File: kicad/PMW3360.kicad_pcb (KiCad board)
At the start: 2 copper layers, 22 x 34 mm, 12 parts, among them J1 Conn_01x07, U1 PMW3360, U2 TCR2EF19

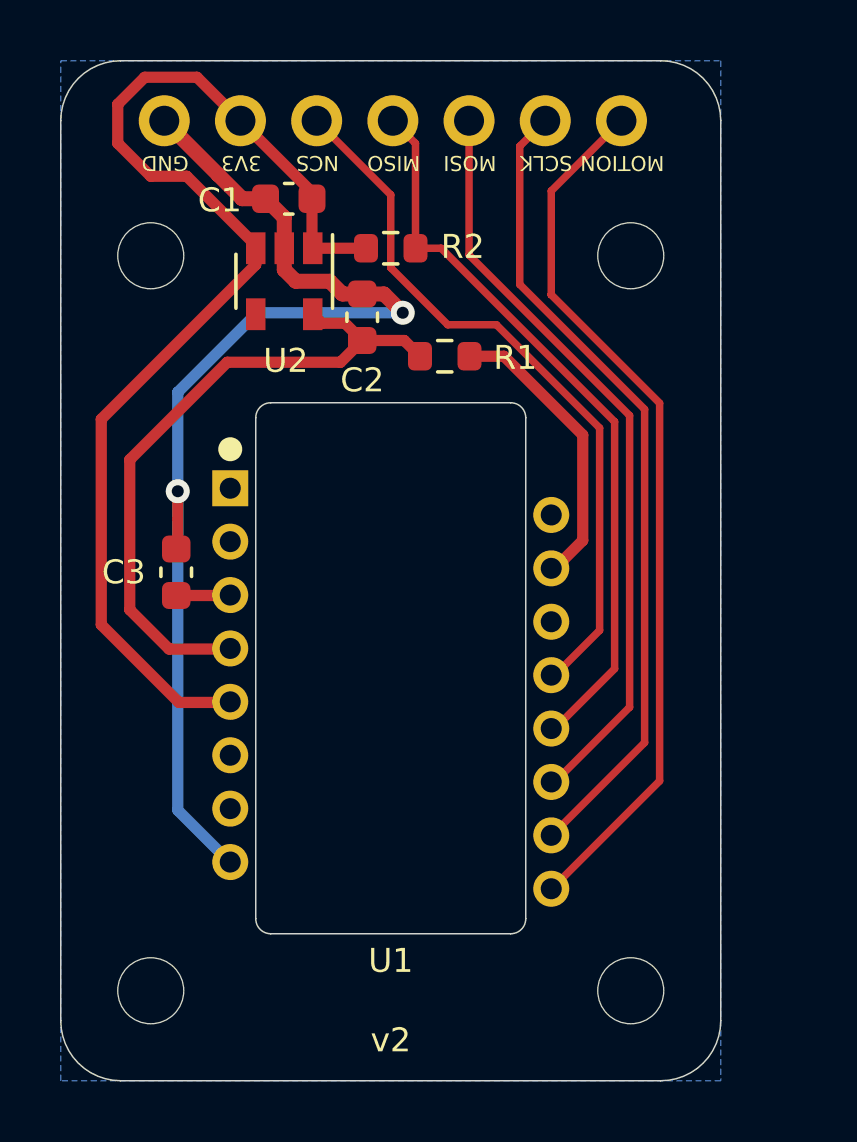
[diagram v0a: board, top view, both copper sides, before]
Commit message: Modified the board dimensions and mounting hole locations to roughly match the old MrJohnK boards from Tindie (22x28mm, with two mounting holes) Changed the connector to a 6-pin JST SH 1.0mm pitch plug with a pinout matching https://en.wikipedia.org/wiki/Pmod_Interface "Type 2 SPI". Edited with KiCad 8.0.7, so the KiCad project files have been updated to its new version file format.
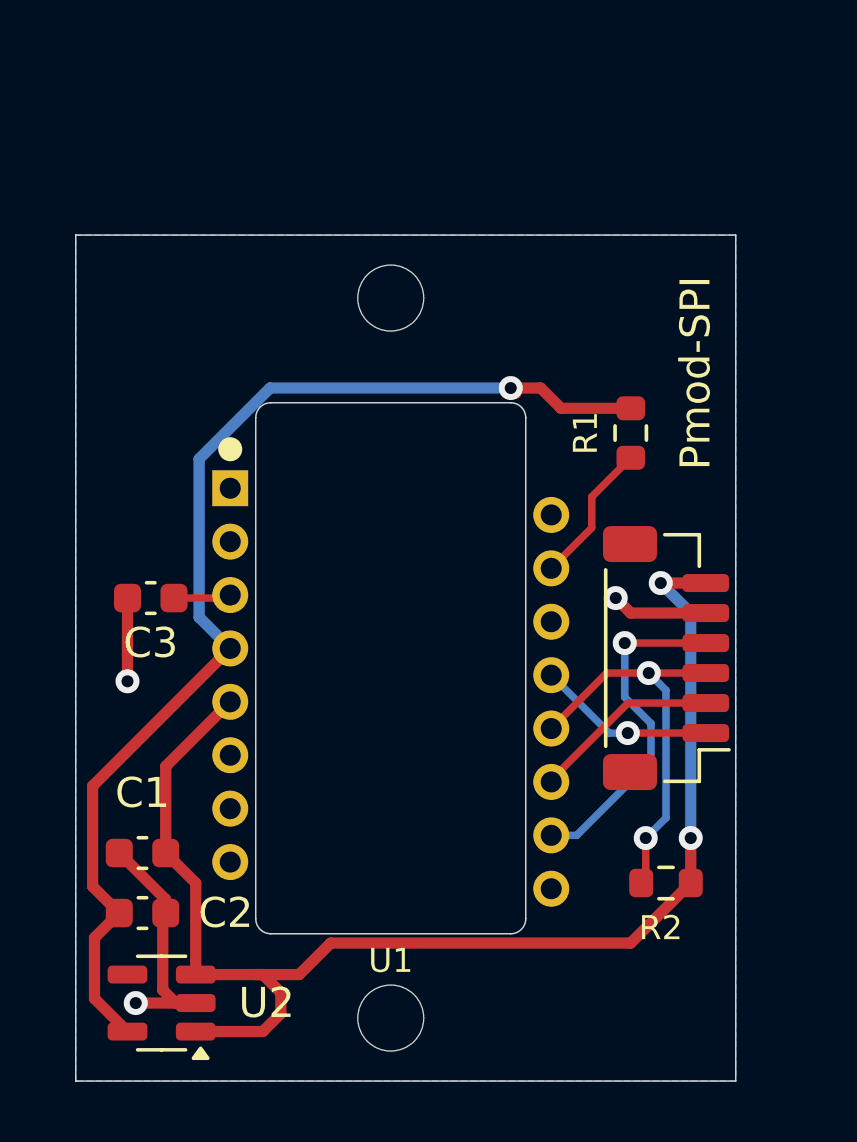
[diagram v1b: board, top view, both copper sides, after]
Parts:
- removed the REF** at (157.0, 117.0)
- removed the REF** at (157.0, 92.5)
- Pmod-SPI: renamed from J1; value Conn_01x07 -> Conn_01x06; footprint Connector_PinHeader_2.54mm:PinHeader_1x07_P2.54mm_Vertical -> Connector_JST:JST_SH_BM06B-SRSS-TB_1x06-1MP_P1.00mm_Vertical
- moved Pmod-SPI 24.5 mm to (158.2, 105.9)
- moved U2 24.4 mm to (141.4, 117.4), turned to 180 degrees
- moved R2 23.1 mm to (158.2, 113.4), turned to 180 degrees
- moved C1 22.3 mm to (140.7, 112.4)
- moved C2 21.2 mm to (140.7, 114.4), turned to 0 degrees
- moved REF** 8.12 mm to (149.0, 93.9)
- moved REF** 8.04 mm to (149.0, 117.8)
- moved R1 6.71 mm to (157.0, 98.4), turned to -90 degrees
- moved C3 1.21 mm to (141.0, 103.9), turned to 180 degrees
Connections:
- Pmod-SPI pad 1: GND -> NCS
- Pmod-SPI pad 2: +3V3 -> MOSI
- Pmod-SPI pad 3: NCS -> MISO
- Pmod-SPI pad 4: MISO -> SCLK
- Pmod-SPI pad 5: MOSI -> GND
- Pmod-SPI pad 6: SCLK -> +3V3
- U1 pad 1: Net-(U1-Pad1) -> unconnected-(U1-NC-Pad1)
- U1 pad 14: Net-(U1-Pad14) -> unconnected-(U1-NC-Pad14)
- U1 pad 16: Net-(U1-Pad16) -> unconnected-(U1-NC-Pad16)
- U1 pad 2: Net-(U1-Pad2) -> unconnected-(U1-NC-Pad2)
- U1 pad 6: Net-(U1-Pad6) -> unconnected-(U1-NC-Pad6)
- U1 pad 7: Net-(U1-Pad7) -> unconnected-(U1-NRESET-Pad7)
- U1 pad 9: MOTION -> unconnected-(U1-MOTION-Pad9)
- U2 pad 4: Net-(U2-Pad4) -> unconnected-(U2-NC-Pad4)
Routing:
- net MOTION: track 29.6 -> 0.00 mm
- net GND: track 38.6 -> 14.7 mm, vias 2 -> 3
- net MOSI: track 25.3 -> 5.81 mm
- net NCS: track 24.5 -> 5.95 mm, vias 0 -> 1
- net +1V8: track 22.4 -> 38.6 mm, vias 0 -> 1
- net SCLK: track 27.2 -> 11.3 mm, vias 0 -> 1
- net MISO: track 24.7 -> 13.7 mm, vias 0 -> 2
- net +3V3: track 39.6 -> 45.3 mm, vias 0 -> 2
- net Net-(U1-LED_P): track 9.72 -> 4.78 mm
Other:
- board size 22 x 34 mm -> 22 x 28.2 mm
- net class Default removed
- net class power removed
- board text removed: "3.3V LOGIC"
- board text removed: "3V3"
- board text removed: "GND"
- board text removed: "MISO"
- board text removed: "MOSI"
- board text removed: "MOTION"
- board text removed: "NCS"
- board text removed: "PMW3360"
- board text removed: "SCLK"
- board text removed: "v2"

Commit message: Switched to JST_GH 1.25mm side-entry plug. Updated part info for the 1.8v regulator to the one that's actually available through JLCPCB.
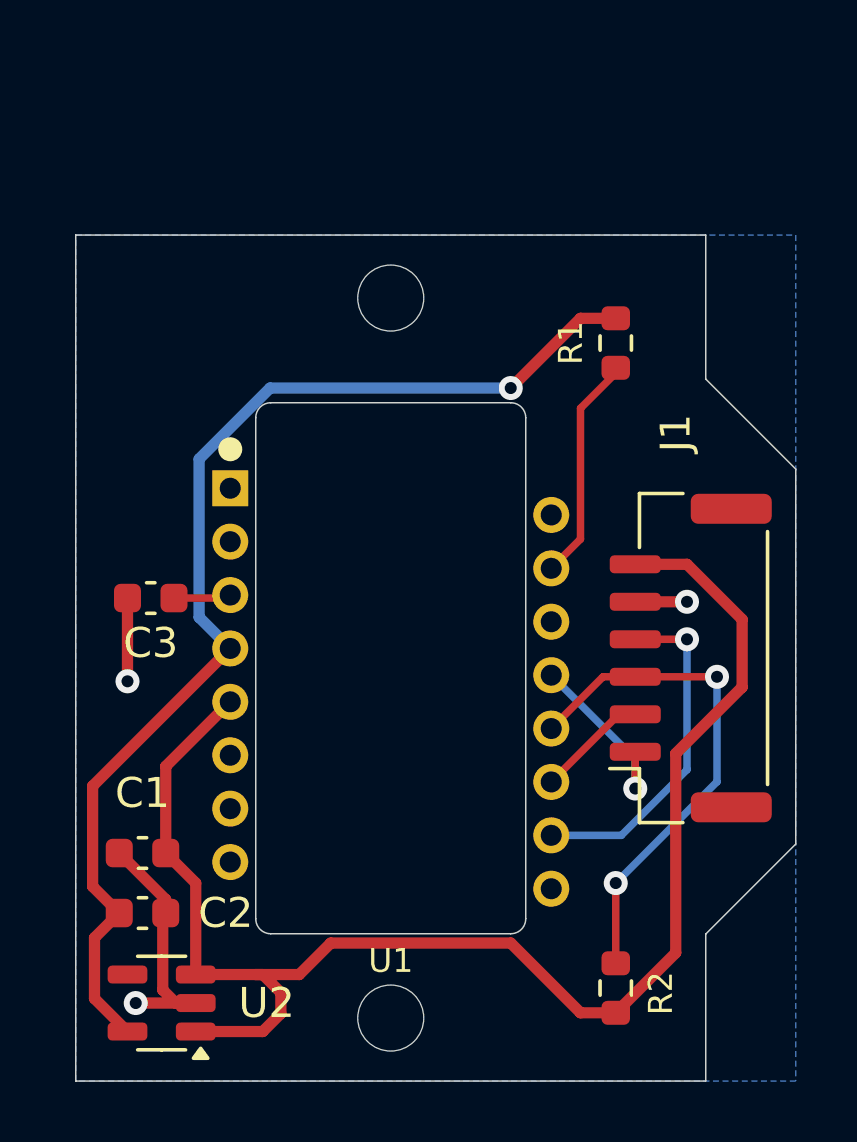
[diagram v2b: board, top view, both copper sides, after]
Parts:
- J1: renamed from Pmod-SPI; footprint Connector_JST:JST_SH_BM06B-SRSS-TB_1x06-1MP_P1.00mm_Vertical -> Connector_JST:JST_GH_SM06B-GHS-TB_1x06-1MP_P1.25mm_Horizontal
- U2: value TCR2EF19 -> TLV70018DDCR
- moved R2 3.88 mm to (156.5, 116.9), turned to -90 degrees
- moved R1 3.04 mm to (156.5, 95.4)
- moved J1 0.82 mm to (159.0, 105.9)
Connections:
- R2 pad 1: +3V3 -> MISO
- R2 pad 2: MISO -> +3V3
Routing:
- net +3V3: track 45.3 -> 50.2 mm, vias 2 -> 0
- net MISO: track 13.7 -> 17.4 mm
- net Net-(U1-LED_P): track 4.78 -> 7.58 mm
- net MOSI: track 5.81 -> 3.80 mm
- net GND: track 14.7 -> 13.2 mm
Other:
- board size 22 x 28.2 mm -> 24 x 28.2 mm

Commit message: Change back to JST SH 1.0mm pitch connector Use top-side 3.3v fill zone for simpler routing add .gitignore file
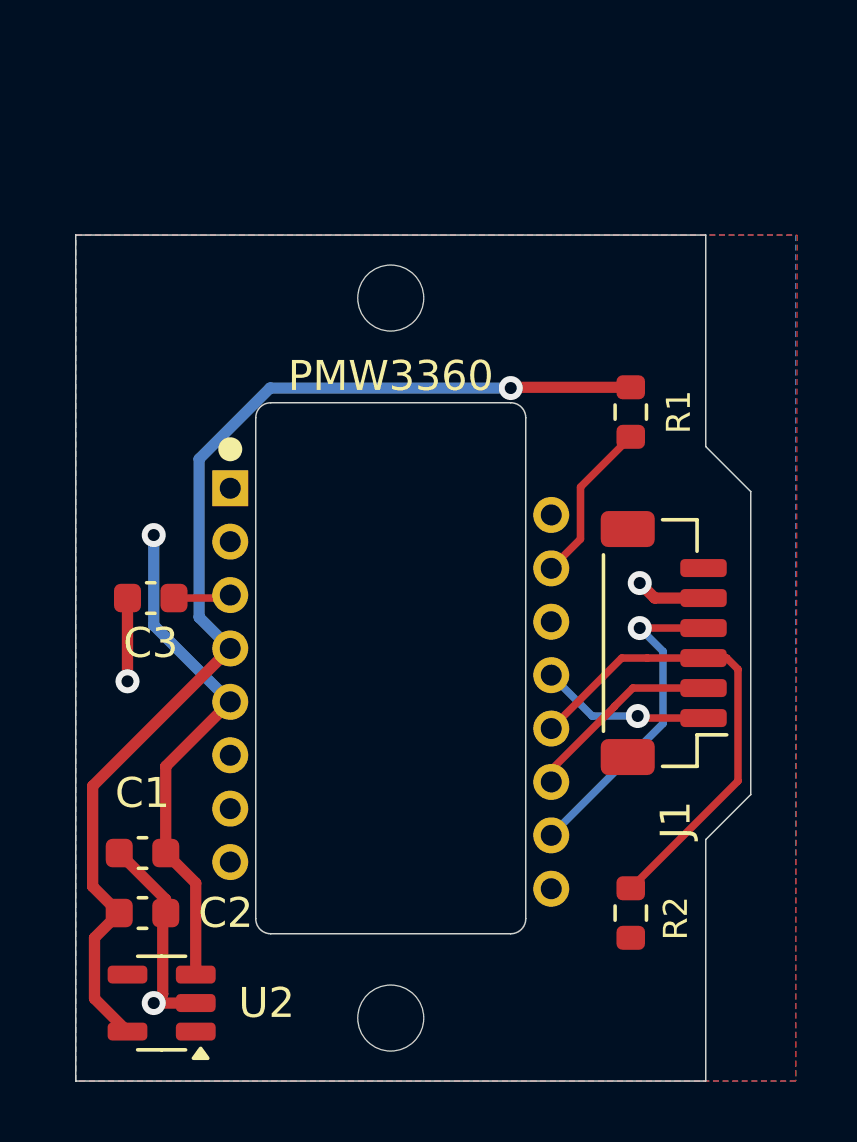
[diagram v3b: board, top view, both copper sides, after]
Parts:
- removed REF** (x2): MountingHole_2.2mm_M2, MountingHole:MountingHole_2.2mm_M2
- added H1: MountingHole, MountingHole:MountingHole_2.2mm_M2, F.Cu at (149.0, 93.9)
- added H2: MountingHole, MountingHole:MountingHole_2.2mm_M2, F.Cu at (149.0, 117.9)
- J1: footprint Connector_JST:JST_GH_SM06B-GHS-TB_1x06-1MP_P1.25mm_Horizontal -> Connector_JST:JST_SH_BM06B-SRSS-TB_1x06-1MP_P1.00mm_Vertical
- moved R2 2.55 mm to (157.0, 114.4)
- moved R1 2.35 mm to (157.0, 97.7)
- moved J1 1.03 mm to (158.1, 105.4)
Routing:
- net +3V3: track 50.2 -> 17.4 mm, vias 0 -> 1
- net MOSI: track 3.80 -> 6.61 mm
- net Net-(U1-LED_P): track 7.58 -> 5.48 mm
- net MISO: track 17.4 -> 16.3 mm, vias 2 -> 0
- net GND: track 13.2 -> 12.5 mm
- net SCLK: track 11.5 -> 10.9 mm
- added copper zone on F.Cu, net +3V3
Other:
- board size 24 x 28.2 mm -> 22.5 x 28.2 mm

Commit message: Update the readme for this fork. Add the url of this github repository to the rear silkscreen layer.
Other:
- board text added: "https://github.com/ monroewilliams/pmw3360-breakout"
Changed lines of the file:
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@@
 		(layer "Edge.Cuts")
+	)
+	(gr_text "https://github.com/\nmonroewilliams/pmw3360-breakout"
+		(at 142.1 105.91 90)
+		(layer "B.SilkS")
+		(effects
+			(font
+				(size 1 1)
+				(thickness 0.15)
+			)
+			(justify bottom mirror)
+		)
 	)
 	(segment

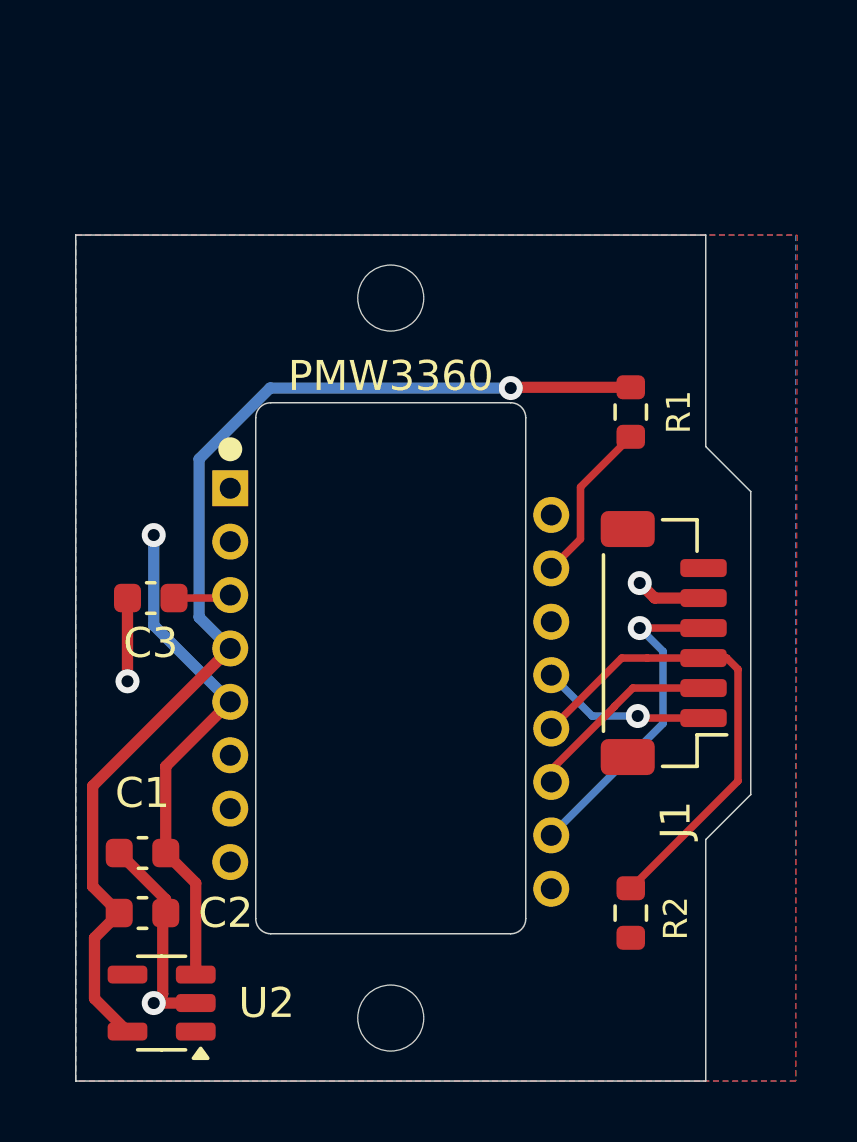
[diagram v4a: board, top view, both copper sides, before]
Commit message: Make more symmetrical. Clean up silkscreens a bit. Add a pad for the motion line.
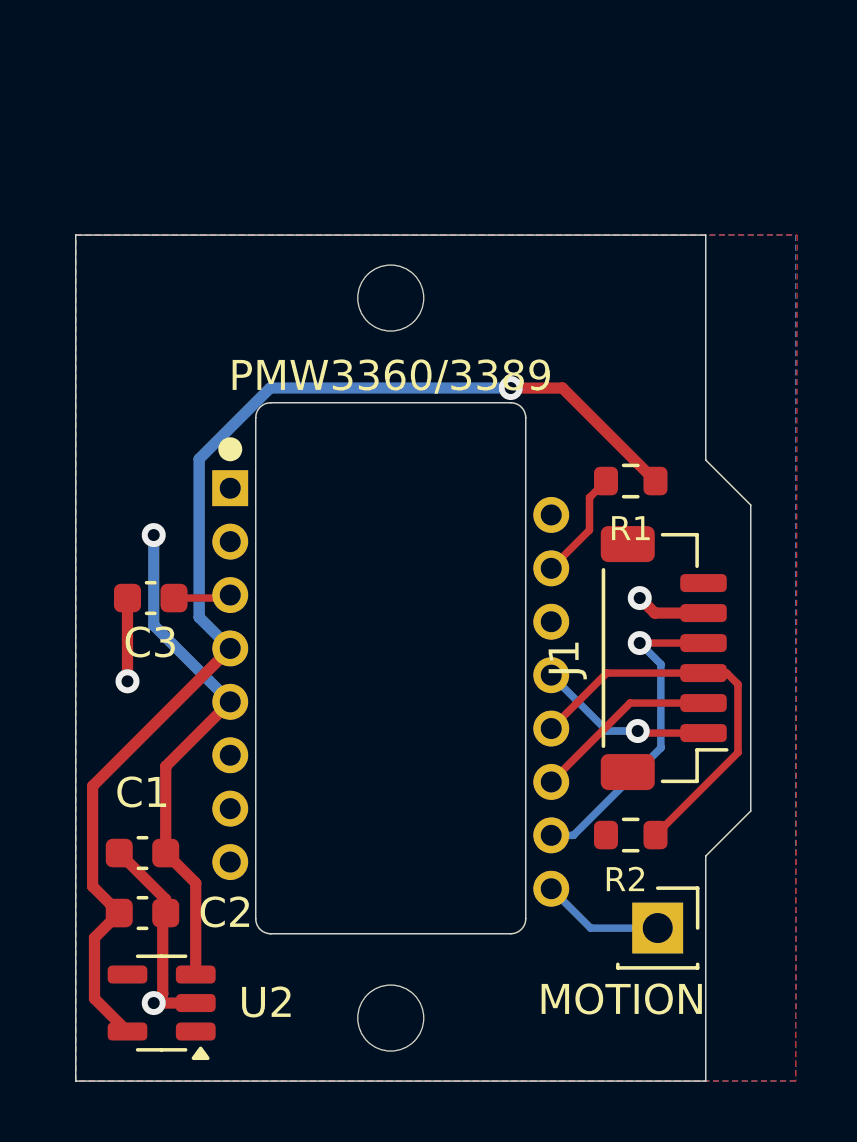
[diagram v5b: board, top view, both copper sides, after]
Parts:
- added J2: MOTION, Connector_PinSocket_2.54mm:PinSocket_1x01_P2.54mm_Vertical, F.Cu at (157.9, 114.9)
- J1: footprint Connector_JST:JST_SH_BM06B-SRSS-TB_1x06-1MP_P1.00mm_Vertical -> PMW3360:JST_SH_BM06B-SRSS-TB_1x06-1MP_P1.00mm_Vertical
- U1: value PMW3360 -> PMW3360/3389
- moved R2 2.60 mm to (157.0, 111.8), turned to 180 degrees
- moved R1 2.30 mm to (157.0, 100.0), turned to 180 degrees
- moved J1 0.50 mm to (158.1, 105.9), turned to -90 degrees
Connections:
- U1 pad 9: unconnected-(U1-MOTION-Pad9) -> Net-(J2-Pin_1)
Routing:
- net Net-(J2-Pin_1): track 0.00 -> 4.09 mm
- net MISO: track 16.3 -> 13.5 mm
- net +1V8: track 38.1 -> 40.2 mm
- net Net-(U1-LED_P): track 5.48 -> 3.67 mm
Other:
- outline, holes or cut-outs redrawn
- board text added: "github.com/monroewilliams/ pmw3360-breakout"
- board text added: "version 1.0"
- board text removed: "https://github.com/ monroewilliams/pmw3360-breakout"
